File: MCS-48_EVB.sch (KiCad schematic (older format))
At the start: 21 parts

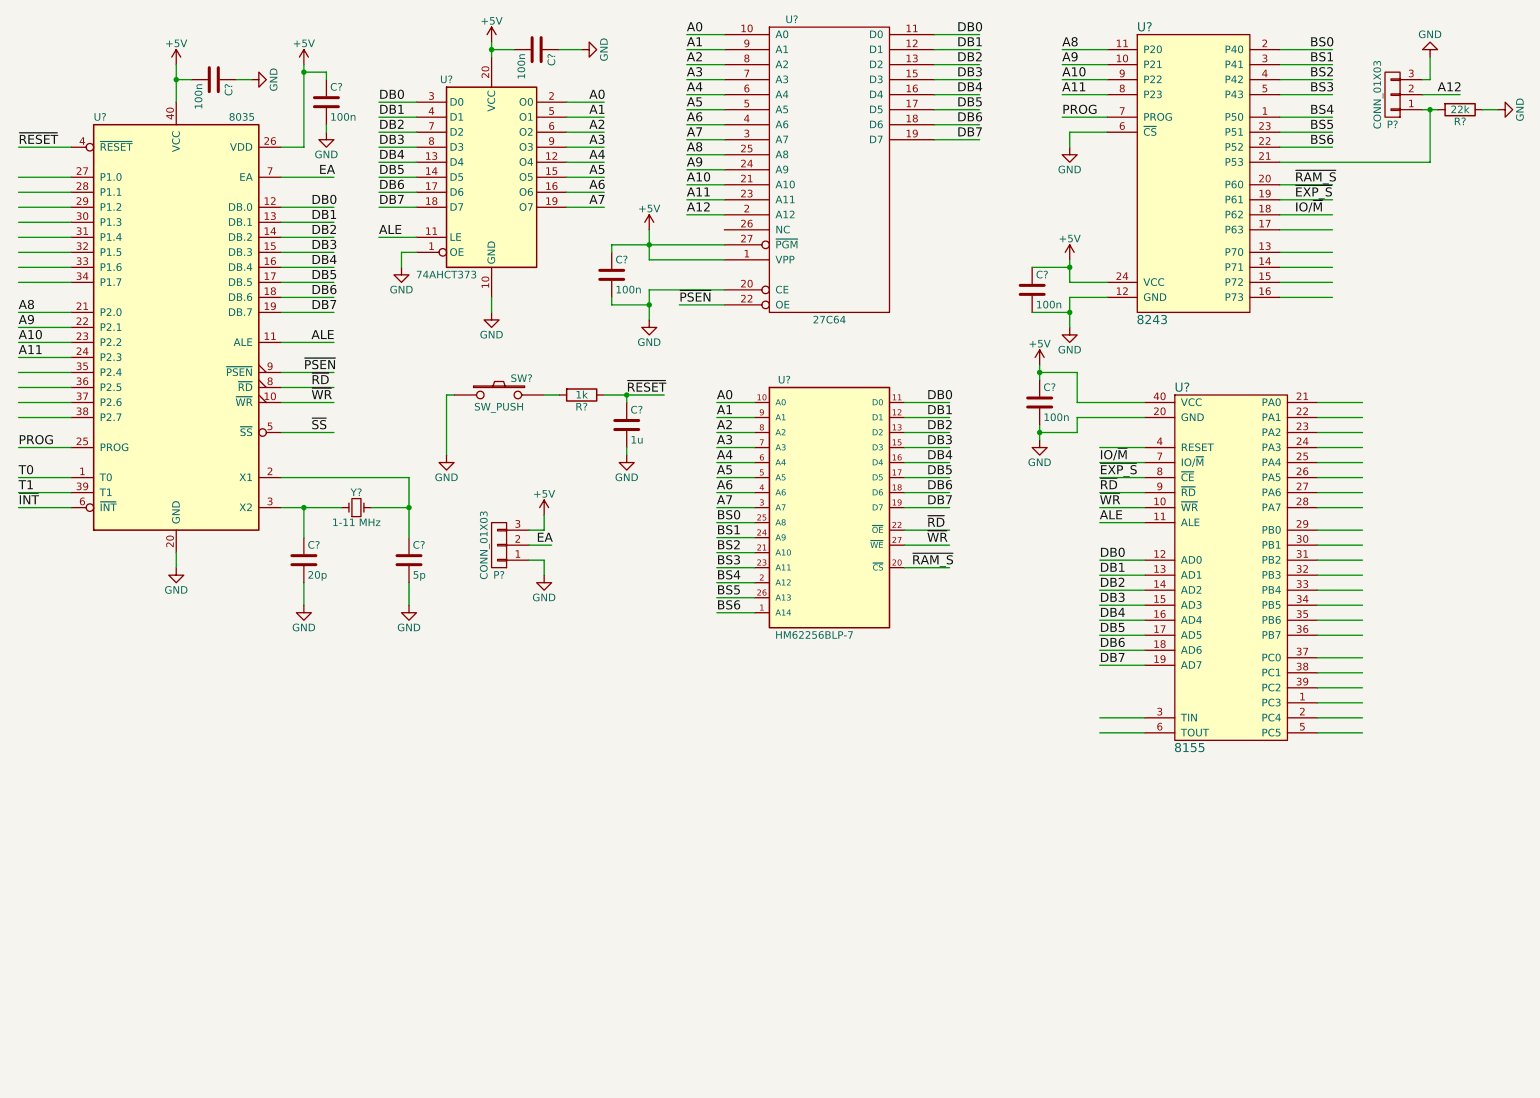
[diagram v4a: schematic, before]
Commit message: Added LCD & keyb conn
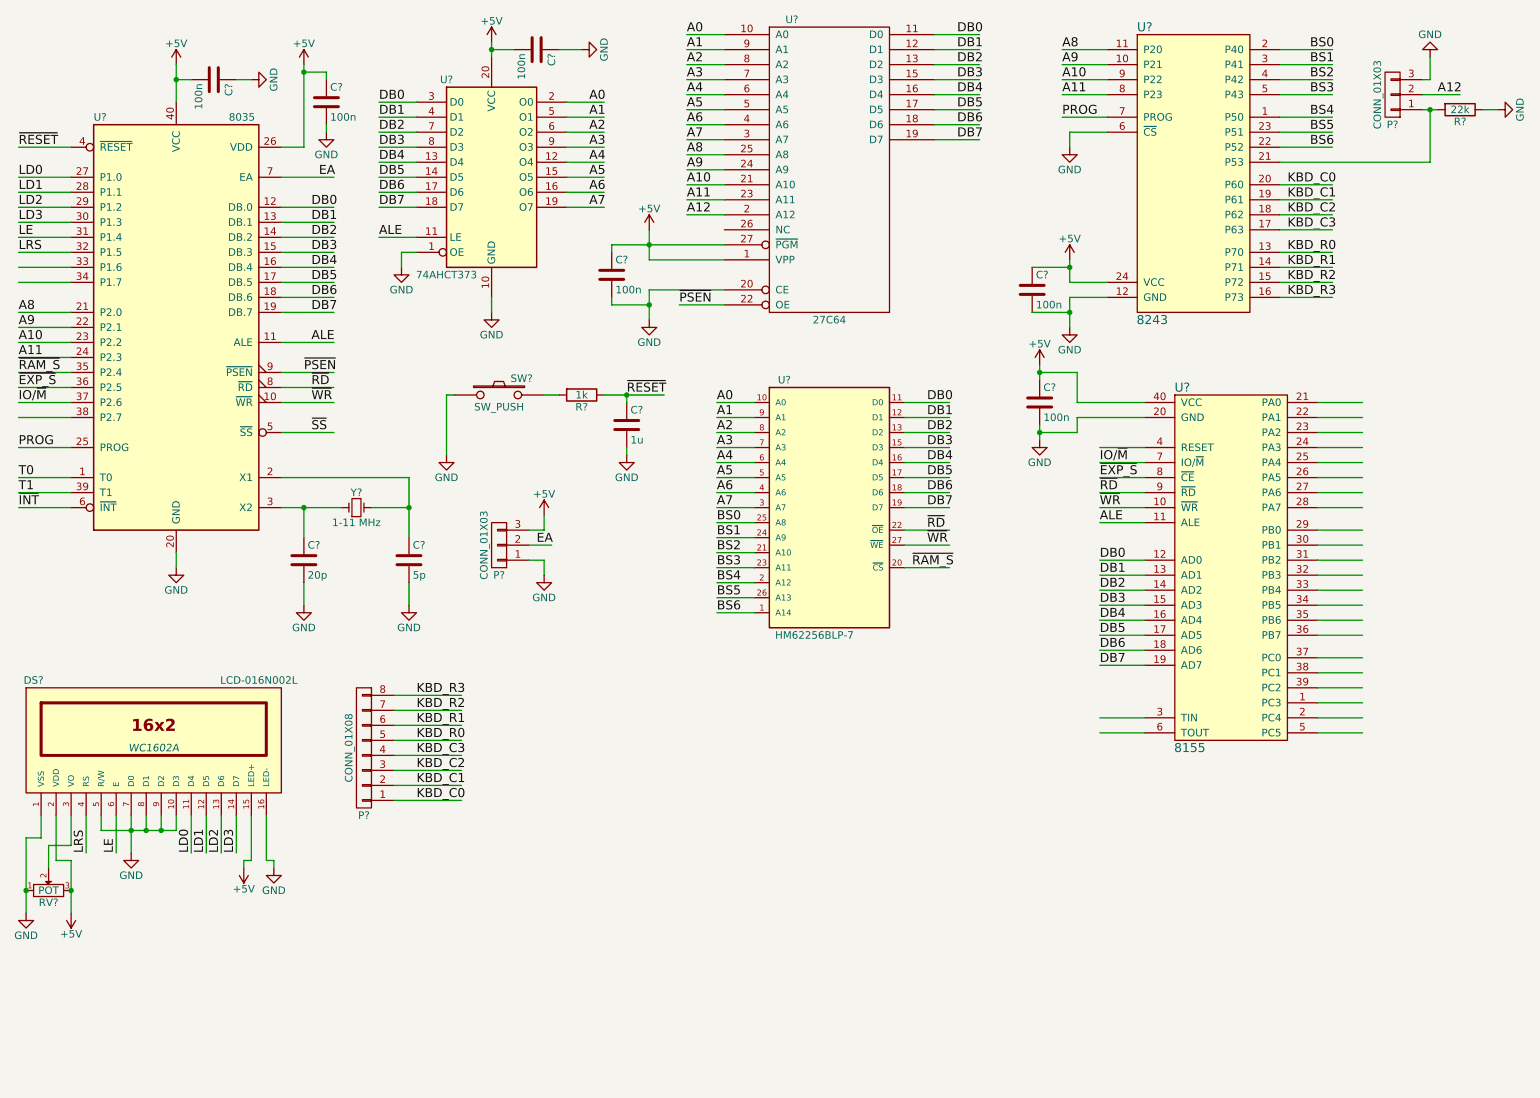
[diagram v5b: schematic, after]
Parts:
- added DS?: LCD-016N002L, WC1602A, symbol LCD-016N002L
- added P?: CONN_01X08, symbol CONN_01X08
- added RV?: POT, symbol POT
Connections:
- net labels added: KBD_C0, KBD_C1, KBD_C2, KBD_C3, KBD_R0, KBD_R1, KBD_R2, KBD_R3, LD0, LD1, LD2, LD3, LE, LRS
- wire segments 222 -> 257
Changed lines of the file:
@@
 Text Label 6700 4250 0    60   ~ 0
 ~RAM_S
-Text Label 9250 1700 0    60   ~ 0
+Text Label 750  2950 0    60   ~ 0
 ~RAM_S
 $Comp
@@
 Text Label 7950 3650 0    60   ~ 0
 ~EXP_S
-Text Label 9250 1800 0    60   ~ 0
+Text Label 750  3050 0    60   ~ 0
 ~EXP_S
-Text Label 9250 1900 0    60   ~ 0
+Text Label 750  3150 0    60   ~ 0
 IO/~M
 Text Label 7950 3550 0    60   ~ 0
@@
 Text Label 7950 4900 0    60   ~ 0
 DB7
+Text Label 9200 1700 0    60   ~ 0
+KBD_C0
+Text Label 9200 1800 0    60   ~ 0
+KBD_C1
+Text Label 9200 1900 0    60   ~ 0
+KBD_C2
+Text Label 9200 2000 0    60   ~ 0
+KBD_C3
+Text Label 9200 2150 0    60   ~ 0
+KBD_R0
+Text Label 9200 2250 0    60   ~ 0
+KBD_R1
+Text Label 9200 2350 0    60   ~ 0
+KBD_R2
+Text Label 9200 2450 0    60   ~ 0
+KBD_R3
+$Comp
+L LCD-016N002L DS?
+U 1 1 63BA0648
+P 1650 5400
+F 0 "DS?" H 850 5800 50  0000 C CNN
+F 1 "LCD-016N002L" H 2350 5800 50  0000 C CNN
+F 2 "WC1602A" H 1650 5350 50  0000 C CIN
+F 3 "" H 1650 5400 50  0000 C CNN
+	1    1650 5400
+	1    0    0    -1
+$EndComp
+$Comp
+L GND #PWR?
+U 1 1 63BA11CB
+P 1500 6150
+F 0 "#PWR?" H 1500 5900 50  0001 C CNN
+F 1 "GND" H 1500 6000 50  0000 C CNN
+F 2 "" H 1500 6150 50  0000 C CNN
+F 3 "" H 1500 6150 50  0000 C CNN
+	1    1500 6150
+	1    0    0    -1
+$EndComp
+Wire Wire Line
+	1500 5900 1500 6150
+Wire Wire Line
+	1300 5900 1300 6000
+Wire Wire Line
+	1300 6000 1800 6000
+Connection ~ 1500 6000
+Wire Wire Line
+	1600 6000 1600 5900
+Wire Wire Line
+	1700 6000 1700 5900
+Connection ~ 1600 6000
+Wire Wire Line
+	1800 6000 1800 5900
+Connection ~ 1700 6000
+Wire Wire Line
+	1900 5900 1900 6150
+Wire Wire Line
+	2000 5900 2000 6150
+Wire Wire Line
+	2100 5900 2100 6150
+Wire Wire Line
+	2200 5900 2200 6150
+Wire Wire Line
+	1400 5900 1400 6150
+Wire Wire Line
+	1200 5900 1200 6150
+Text Label 1400 6150 1    60   ~ 0
+LE
+Text Label 1200 6150 1    60   ~ 0
+LRS
+Text Label 1900 6150 1    60   ~ 0
+LD0
+Text Label 2000 6150 1    60   ~ 0
+LD1
+Text Label 2100 6150 1    60   ~ 0
+LD2
+Text Label 2200 6150 1    60   ~ 0
+LD3
+Text Label 750  1650 0    60   ~ 0
+LD0
+Text Label 750  1750 0    60   ~ 0
+LD1
+Text Label 750  1850 0    60   ~ 0
+LD2
+Text Label 750  1950 0    60   ~ 0
+LD3
+Text Label 750  2050 0    60   ~ 0
+LE
+Text Label 750  2150 0    60   ~ 0
+LRS
+$Comp
+L POT RV?
+U 1 1 63BA2D15
+P 950 6400
+F 0 "RV?" H 950 6320 50  0000 C CNN
+F 1 "POT" H 950 6400 50  0000 C CNN
+F 2 "" H 950 6400 50  0000 C CNN
+F 3 "" H 950 6400 50  0000 C CNN
+	1    950  6400
+	1    0    0    -1
+$EndComp
+Wire Wire Line
+	950  6250 950  6100
+Wire Wire Line
+	950  6100 1100 6100
+Wire Wire Line
+	1100 6100 1100 5900
+Wire Wire Line
+	800  6050 800  6550
+Wire Wire Line
+	800  6050 900  6050
+Wire Wire Line
+	900  6050 900  5900
+Wire Wire Line
+	1100 6200 1100 6550
+Wire Wire Line
+	1100 6200 1000 6200
+Wire Wire Line
+	1000 6200 1000 5900
+$Comp
+L GND #PWR?
+U 1 1 63BA3334
+P 800 6550
+F 0 "#PWR?" H 800 6300 50  0001 C CNN
+F 1 "GND" H 800 6400 50  0000 C CNN
+F 2 "" H 800 6550 50  0000 C CNN
+F 3 "" H 800 6550 50  0000 C CNN
+	1    800  6550
+	1    0    0    -1
+$EndComp
+$Comp
+L +5V #PWR?
+U 1 1 63BA3376
+P 1100 6550
+F 0 "#PWR?" H 1100 6400 50  0001 C CNN
+F 1 "+5V" H 1100 6690 50  0000 C CNN
+F 2 "" H 1100 6550 50  0000 C CNN
+F 3 "" H 1100 6550 50  0000 C CNN
+	1    1100 6550
+	-1   0    0    1
+$EndComp
+Connection ~ 800  6400
+Connection ~ 1100 6400
+$Comp
+L +5V #PWR?
+U 1 1 63BA3776
+P 2250 6250
+F 0 "#PWR?" H 2250 6100 50  0001 C CNN
+F 1 "+5V" H 2250 6390 50  0000 C CNN
+F 2 "" H 2250 6250 50  0000 C CNN
+F 3 "" H 2250 6250 50  0000 C CNN
+	1    2250 6250
+	-1   0    0    1
+$EndComp
+$Comp
+L GND #PWR?
+U 1 1 63BA37D1
+P 2450 6250
+F 0 "#PWR?" H 2450 6000 50  0001 C CNN
+F 1 "GND" H 2450 6100 50  0000 C CNN
+F 2 "" H 2450 6250 50  0000 C CNN
+F 3 "" H 2450 6250 50  0000 C CNN
+	1    2450 6250
+	1    0    0    -1
+$EndComp
+Wire Wire Line
+	2250 6250 2250 6200
+Wire Wire Line
+	2250 6200 2300 6200
+Wire Wire Line
+	2300 6200 2300 5900
+Wire Wire Line
+	2450 6250 2450 6200
+Wire Wire Line
+	2450 6200 2400 6200
+Wire Wire Line
+	2400 6200 2400 5900
+$Comp
+L CONN_01X08 P?
+U 1 1 63BA3F9F
+P 3050 5450
+F 0 "P?" H 3050 5900 50  0000 C CNN
+F 1 "CONN_01X08" V 3150 5450 50  0000 C CNN
+F 2 "" H 3050 5450 50  0000 C CNN
+F 3 "" H 3050 5450 50  0000 C CNN
+	1    3050 5450
+	-1   0    0    1
+$EndComp
+Wire Wire Line
+	3250 5800 3700 5800
+Wire Wire Line
+	3250 5700 3700 5700
+Wire Wire Line
+	3250 5600 3700 5600
+Wire Wire Line
+	3250 5500 3700 5500
+Wire Wire Line
+	3250 5400 3700 5400
+Wire Wire Line
+	3250 5300 3700 5300
+Wire Wire Line
+	3250 5200 3700 5200
+Wire Wire Line
+	3250 5100 3700 5100
+Text Label 3400 5800 0    60   ~ 0
+KBD_C0
+Text Label 3400 5700 0    60   ~ 0
+KBD_C1
+Text Label 3400 5600 0    60   ~ 0
+KBD_C2
+Text Label 3400 5500 0    60   ~ 0
+KBD_C3
+Text Label 3400 5400 0    60   ~ 0
+KBD_R0
+Text Label 3400 5300 0    60   ~ 0
+KBD_R1
+Text Label 3400 5200 0    60   ~ 0
+KBD_R2
+Text Label 3400 5100 0    60   ~ 0
+KBD_R3
 $EndSCHEMATC

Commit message: Added connectors. Power connector and step mode circuit left.
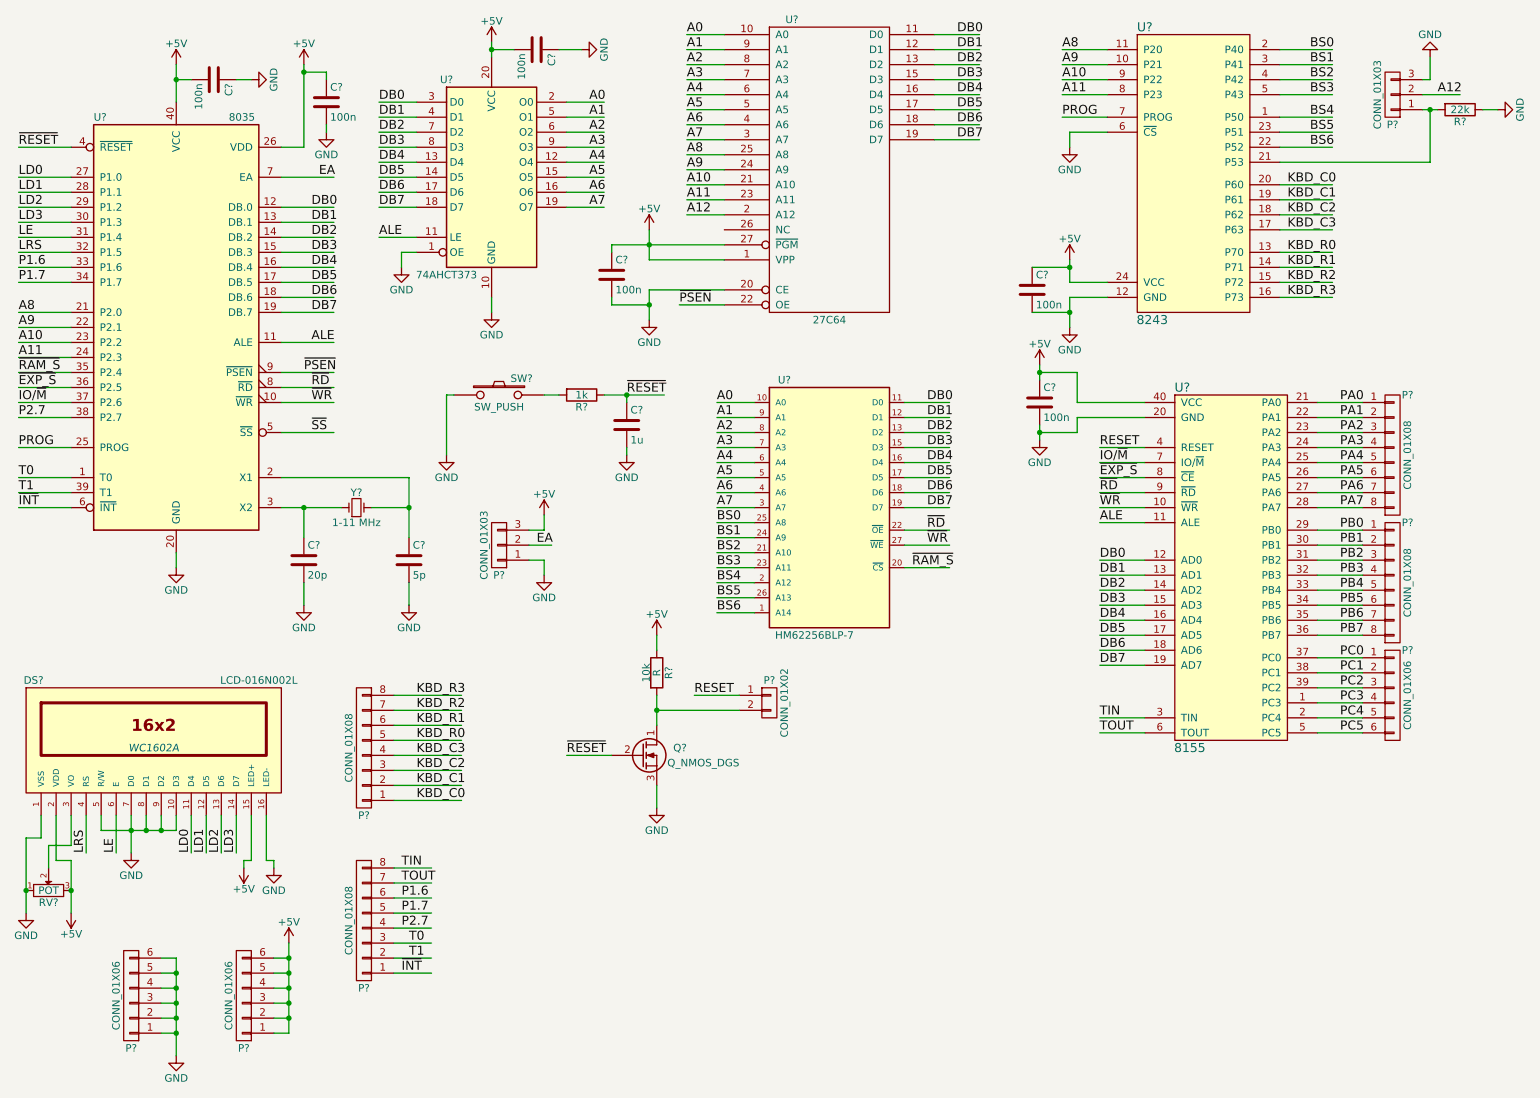
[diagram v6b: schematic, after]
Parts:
- added P? (x3): CONN_01X08, symbol CONN_01X08
- added P? (x3): CONN_01X06, symbol CONN_01X06
- added P?: CONN_01X02, symbol CONN_01X02
- added Q?: Q_NMOS_DGS, symbol Q_NMOS_DGS
- added R?: R, 10k, symbol R
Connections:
- net labels added: P1.6, P1.7, P2.7, PA0, PA1, PA2, PA3, PA4, PA5, PA6, PA7, PB0, PB1, PB2, PB3, PB4, PB5, PB6, PB7, PC0, PC1, PC2, PC3, PC4, PC5, RESET, TIN, TOUT
- wire segments 257 -> 285

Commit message: Started working on PCB.
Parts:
- added C8: 100u, Capacitors_ThroughHole:CP_Radial_D6.3mm_P2.50mm, symbol CP
- added CON1: BARREL_JACK, Connect:BARREL_JACK, symbol BARREL_JACK
- added P5: CONN_01X03, Pin_Headers:Pin_Header_Straight_1x03_Pitch2.54mm, symbol CONN_01X03
- C1, C10, C2, C3, C4, C5, C6, C7, C9: renamed from C?; footprint (none) -> Capacitors_SMD:C_0805_HandSoldering
- DS1: renamed from DS?; footprint WC1602A -> Display:WC1602A
- P1, P11, P2: renamed from P?; footprint (none) -> Pin_Headers:Pin_Header_Straight_1x06_Pitch2.54mm
- P10, P3, P4, P9: renamed from P?; footprint (none) -> Pin_Headers:Pin_Header_Straight_1x08_Pitch2.54mm
- P6, P8: renamed from P?; footprint (none) -> Pin_Headers:Pin_Header_Straight_1x03_Pitch2.54mm
- P7: renamed from P?; footprint (none) -> Pin_Headers:Pin_Header_Straight_1x02_Pitch2.54mm
- Q1: renamed from Q?; footprint (none) -> TO_SOT_Packages_THT:TO-92_Inline_Narrow_Oval
- R1, R3: renamed from R?; footprint (none) -> Resistors_SMD:R_0805_HandSoldering
- R2: renamed from R?; value R -> 10k; footprint 10k -> Resistors_SMD:R_0805_HandSoldering
- RV1: renamed from RV?; value POT -> 10k; footprint (none) -> Potentiometers:Potentiometer_Trimmer_ACP_CA9v_Horizontal_Px10.0mm_Py5.0mm
- SW1: renamed from SW?; footprint (none) -> Buttons_Switches_ThroughHole:SW_PUSH_6mm
- Y1: renamed from Y?; footprint (none) -> Crystals:Crystal_HC18-U_Vertical
- gave numbers to parts that had none: 6
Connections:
- wire segments 285 -> 298
- no-connect marks 0 -> 1

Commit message: Finished component placement.
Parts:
- added C11: 100n, Capacitors_SMD:C_0805_HandSoldering, symbol C
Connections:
- wire segments 298 -> 300
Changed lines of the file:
@@
 	2950 3450 2950 2750
 NoConn ~ 5450 2000
+$Comp
+L C C11
+U 1 1 63BC55A7
+P 7250 4300
+F 0 "C11" H 7275 4400 50  0000 L CNN
+F 1 "100n" H 7275 4200 50  0000 L CNN
+F 2 "Capacitors_SMD:C_0805_HandSoldering" H 7288 4150 50  0001 C CNN
+F 3 "" H 7250 4300 50  0000 C CNN
+	1    7250 4300
+	1    0    0    -1
+$EndComp
+$Comp
+L GND #PWR?
+U 1 1 63BC5651
+P 7250 4550
+F 0 "#PWR?" H 7250 4300 50  0001 C CNN
+F 1 "GND" H 7250 4400 50  0000 C CNN
+F 2 "" H 7250 4550 50  0000 C CNN
+F 3 "" H 7250 4550 50  0000 C CNN
+	1    7250 4550
+	1    0    0    -1
+$EndComp
+$Comp
+L +5V #PWR?
+U 1 1 63BC56AF
+P 7250 4050
+F 0 "#PWR?" H 7250 3900 50  0001 C CNN
+F 1 "+5V" H 7250 4190 50  0000 C CNN
+F 2 "" H 7250 4050 50  0000 C CNN
+F 3 "" H 7250 4050 50  0000 C CNN
+	1    7250 4050
+	1    0    0    -1
+$EndComp
+Wire Wire Line
+	7250 4050 7250 4150
+Wire Wire Line
+	7250 4450 7250 4550
 $EndSCHEMATC
